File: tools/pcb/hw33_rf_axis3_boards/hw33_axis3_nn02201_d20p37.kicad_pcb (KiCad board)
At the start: 2 copper layers, 20.4 x 20.4 mm, 6 parts, among them J1 U.FL-R-SMT-1

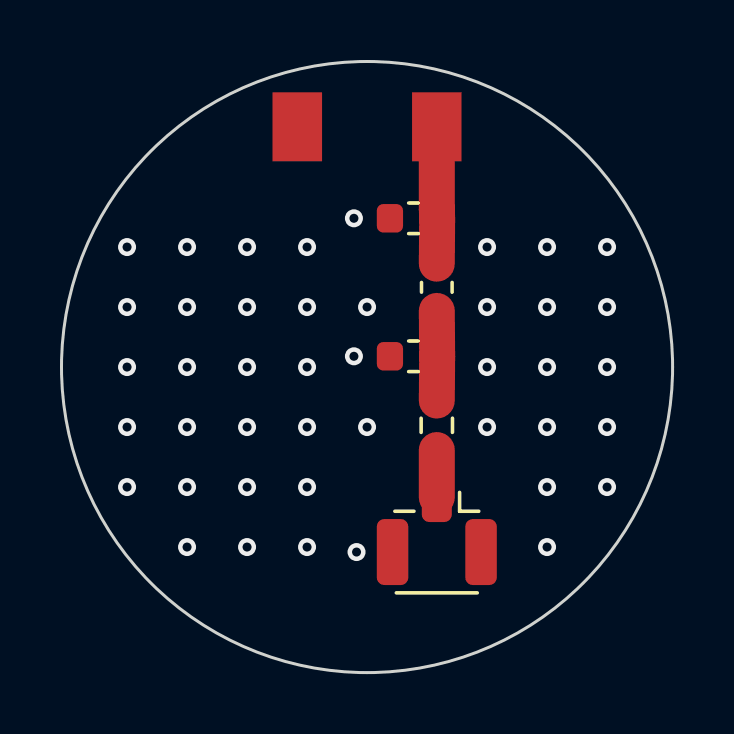
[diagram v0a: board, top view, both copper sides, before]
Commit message: HW.33 · фікси за адверсаром 037b77bc3: стартова мережа — Т із CR80, «П-ланка» знята як хибна топологія, корпус бустера — у перевірці контуру
Адверсар знайшов, що моя ж дописка «eval-ланка — Г, не П» узагальнила одну
плату з трьох: AN_NN02-224_ISM має в нашій смузі Г на 131 × 60 (863–870), Т на
131 × 60 (863–928) і Т на CR80 86 × 54 (863–870; 30 · 13 шунт · 3 nH) — а CR80
найближча до нашої землі. Звірено рендером сторінки 19. Стартова точка тюнінгу
тепер — Т на сайтах B · C · D (аркуш стенда §5, README, шапка генератора).

Звідси клас ширший за дописку: «П-ланка» стояла в 14 місцях канону, трекера й
аркушів, а 02_01 §5.3 називав «посадкові місця під П-ланку» вимогою «обох
app-note дослівно» — app-note каже «matching network», топології не називаючи,
а в прочитаних мережах NN02-224 П немає жодного разу; П-посадка Т не вміщає.
Назва — за функцією («узгоджувальна ланка») скрізь; у домі вимоги (02_01 §5.3)
і в 👤-нозі розкладки HW.9 — заборона «не під П-ланку» з підставою.

Генератор: корпус бустера — частина розміщення й перевірки контуру (корпус
NN02-201 7.0 × 3.0 ширший за пади й стояв 0.05 мм від краю — UM_NN02-201 §2.1);
провенанс NN02-201 — sha256 і власний посібник (монтажний пад «must NOT be
grounded», стор. 11); вертикальна ланка зсунута на 1 мм до центру, щоб U.FL
лишився в контурі; паркан via може заходити в кортьярди деталей ланки (не в
пади); плата, що не пройшла DRC, видаляється разом із проєктом; площа
clearance-сегмента друкується — 30–33 % диска для NN02-224, 18–20 % для NN02-201
(«найвужча» ≠ «мала»: тепер це сказано числом у README, аркуші й нозі).

Тексти, що казали сильніше за плату, приведено до виміру: «via біля кожного
GND-паду» — неправда для U.FL на трьох платах (другий пад — 3–4 мм, λ_g/50);
«≈ λ/22» — число доби Ø15.57, на наших дисках λ/17–18 (і в домі числа 02_01 §5.3
— дописка); набір для тюнінгу — з деталей, які називає сам виробник (LQW18AN 0603,
LQW15AN і GJM1555 0402), а не з памʼяті.

Ще два члени класу: калькулятор площі рахує кортьяр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
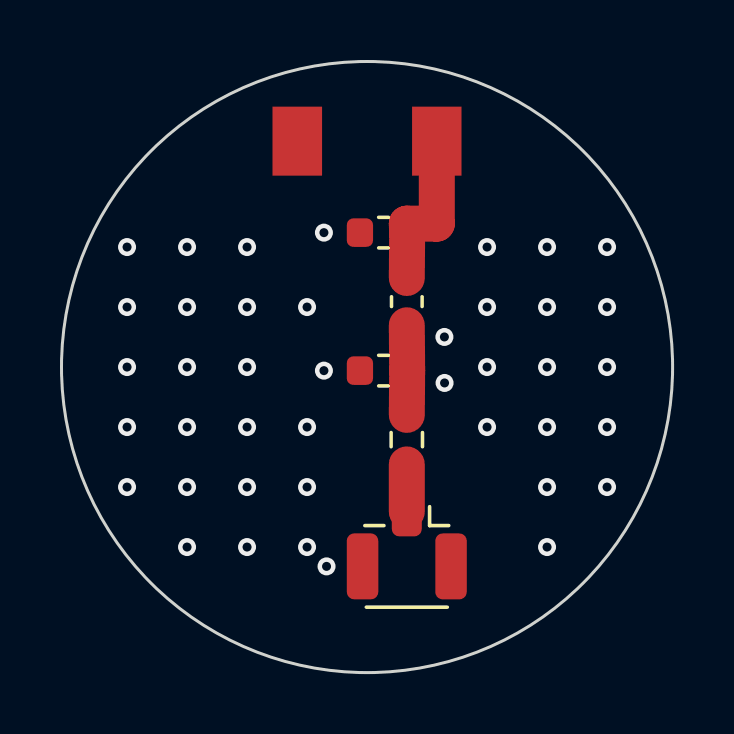
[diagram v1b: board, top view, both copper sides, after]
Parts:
- moved B 1.11 mm to (1.32, -2.18)
- moved D 1.11 mm to (1.32, 2.42)
- moved J1 1.11 mm to (1.32, 6.64)
- moved A 1.11 mm to (0.55, -4.48)
- moved C 1.11 mm to (0.55, 0.12)
- moved AE1 0.48 mm to (0.00, -7.53)
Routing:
- net ANT: track 4.56 -> 5.56 mm
- net GND: vias 43 -> 41
